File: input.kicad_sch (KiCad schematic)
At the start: 4 parts

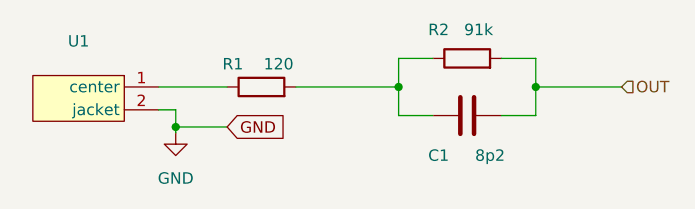
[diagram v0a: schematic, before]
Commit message: ufl connector
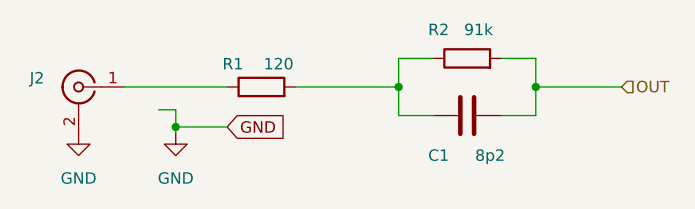
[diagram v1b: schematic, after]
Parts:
- removed U1: ~, solder_coax:solder_coax, symbol pcie_x1:solver_coax
- added J2: IPEX-004, Connector_Coaxial:U.FL_Molex_MCRF_73412-0110_Vertical, symbol Connector:Conn_Coaxial
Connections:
- net GND: now also J2.2 (Ext)
- net at R1.1: now also J2.1 (In)

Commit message: rj45 version of the logic analyzer
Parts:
- J2: footprint Connector_Coaxial:U.FL_Molex_MCRF_73412-0110_Vertical -> Connector_Coaxial:SMA_Amphenol_132289_EdgeMount
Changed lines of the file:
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@@
 			)
 		)
-		(property "Footprint" "Connector_Coaxial:U.FL_Molex_MCRF_73412-0110_Vertical"
+		(property "Footprint" "Connector_Coaxial:SMA_Amphenol_132289_EdgeMount"
 			(at 72.39 68.58 0)
 			(effects
@@
 			)
 		)
-		(property "Datasheet" " ~"
+		(property "Datasheet" "~"
 			(at 72.39 68.58 0)
 			(effects
